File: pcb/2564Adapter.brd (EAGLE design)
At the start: 35.6 x 21.6 mm, 6 parts, among them IC1 TMS2564, IC2 EPROM

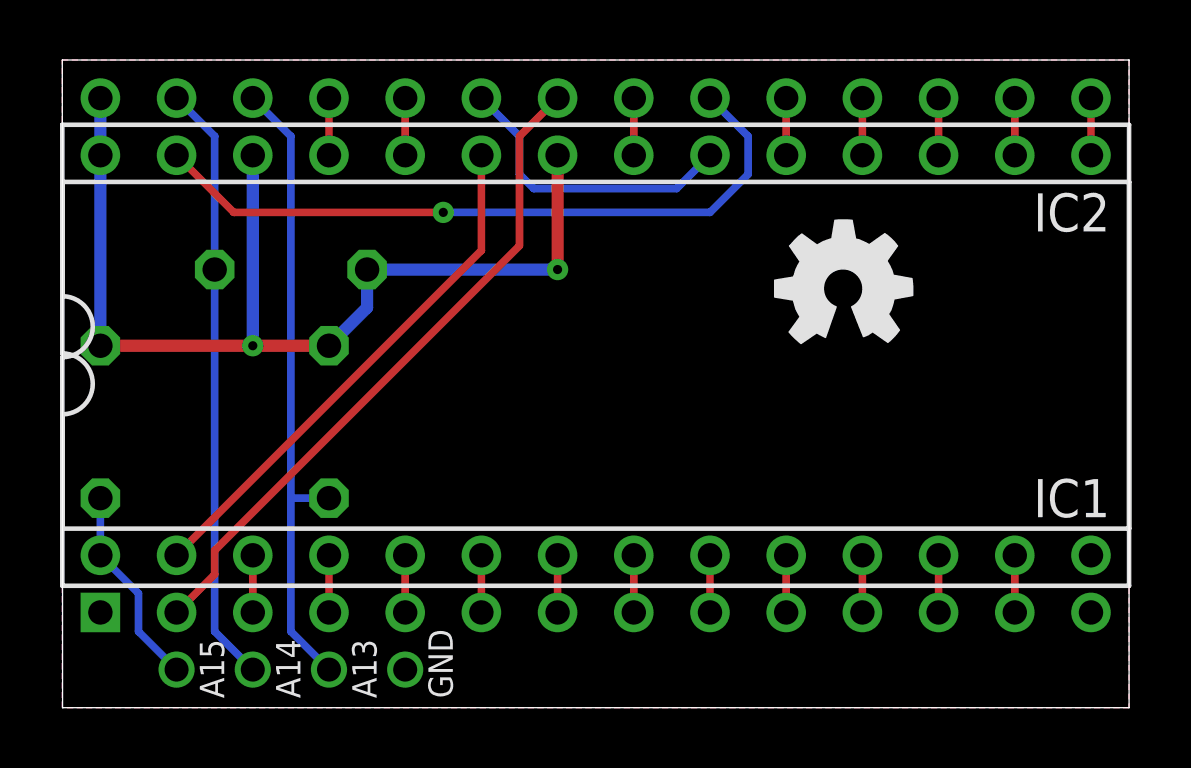
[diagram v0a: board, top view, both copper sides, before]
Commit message: !PGM/PD is a possible select pin, so add in required logic to handle correctly for all cases.
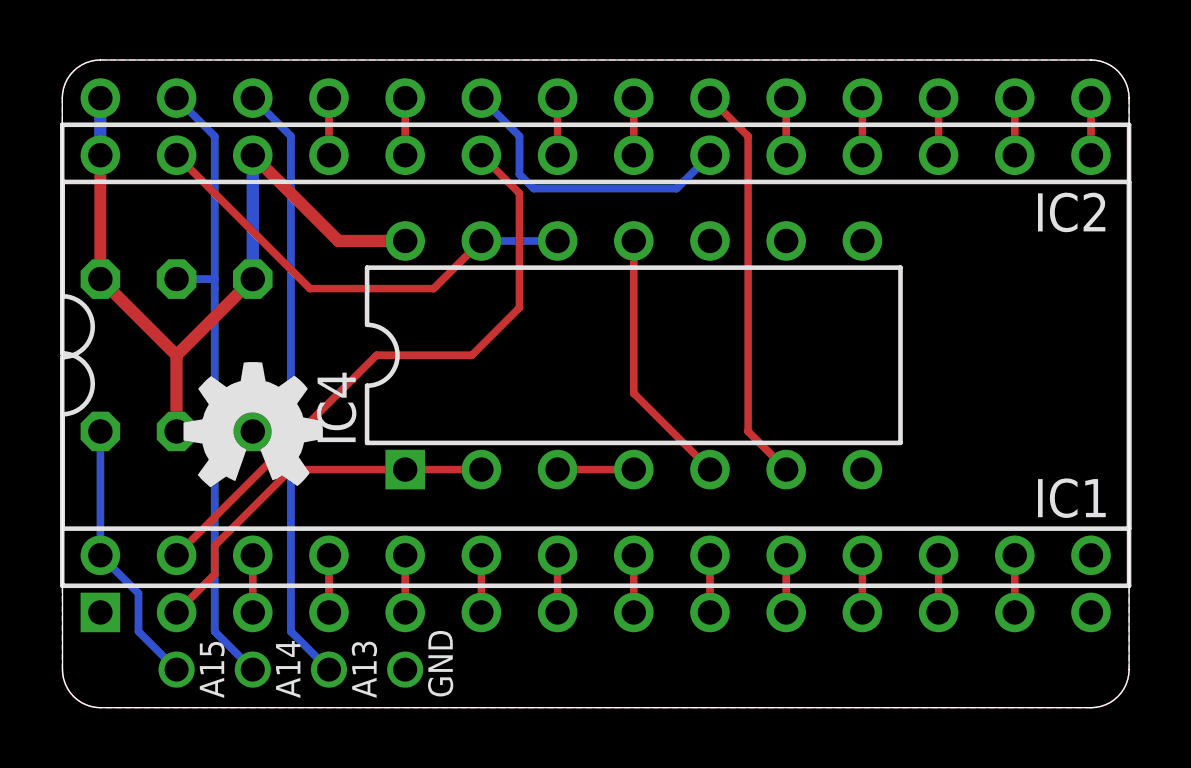
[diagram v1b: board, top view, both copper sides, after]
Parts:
- added IC4: 74LS00N, 74xx-us-jlb:DIL14-RP
- moved GOLD_ORB_SM1 20.3 mm to (6.35, 9.21)
- moved R2 4.76 mm to (3.81, 11.7), turned to 270 degrees
- moved R1 3.38 mm to (6.35, 11.7)
- moved R3 2.22 mm to (1.27, 11.7)
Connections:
- removed net N$3: IC1.2, IC2.22
- new net !CE: IC2.20, IC4.6
- new net !CS1: IC1.2, IC4.1, IC4.2
- new net !CS2: IC1.27, IC4.12, IC4.13
- new net N$2: IC4.11, IC4.5
- new net PD: IC1.22, IC2.22
- net GND: now also IC4.10, IC4.7, IC4.9
- net N$1: now also IC4.3, IC4.4; no longer IC1.27, IC2.20
- net VCC: now also IC4.14; no longer IC1.22
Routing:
- net N$3: track 22.4 -> 0.00 mm
- net N$1: track 23.4 -> 2.54 mm, vias 1 -> 0
- net !CS2: track 0.00 -> 15.2 mm
- net !CE: track 0.00 -> 13.4 mm
- net !CS1: track 0.00 -> 12.7 mm
- net VCC: track 35.5 -> 26.1 mm, vias 2 -> 0
- net N$2: track 0.00 -> 8.67 mm
- net A12: track 17.5 -> 20.5 mm
- net A15: track 6.77 -> 8.99 mm
- net PD: track 0.00 -> 1.91 mm
- net A14: track 20.1 -> 21.4 mm
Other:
- outline, holes or cut-outs redrawn
- board text added: "(c) 2018-19 RETRO Innovations"
- board text removed: "(c) 2018 RETRO Innovations"
